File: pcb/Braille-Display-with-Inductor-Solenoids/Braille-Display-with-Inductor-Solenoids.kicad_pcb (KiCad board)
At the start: 2 copper layers, 58.2 x 57.4 mm, 56 parts, among them J1 Screw_Terminal_01x02, J2 Screw_Terminal_01x02, J3 Screw_Terminal_01x02, U1 RP2040-Zero, U2 TPIC6595, U3 TPIC6595, U4 TPIC6595

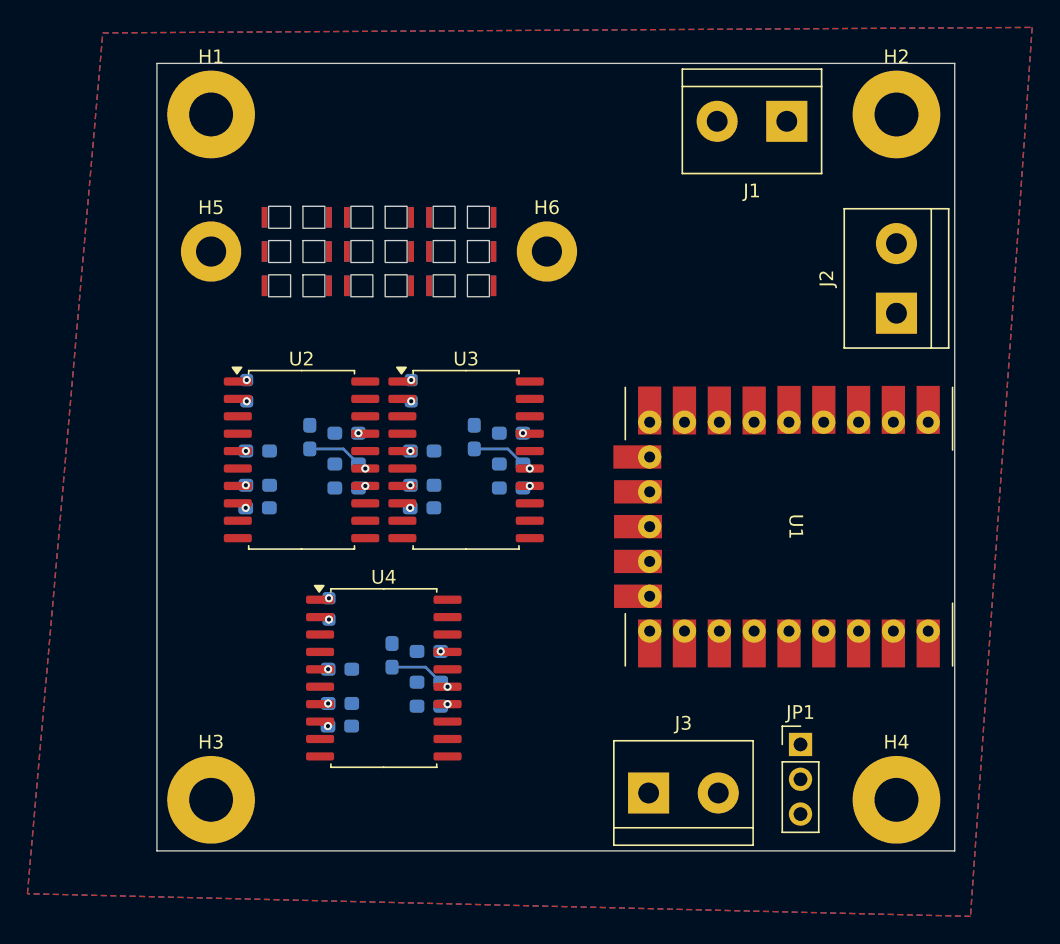
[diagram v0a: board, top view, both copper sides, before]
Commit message: Update net class rules for routing
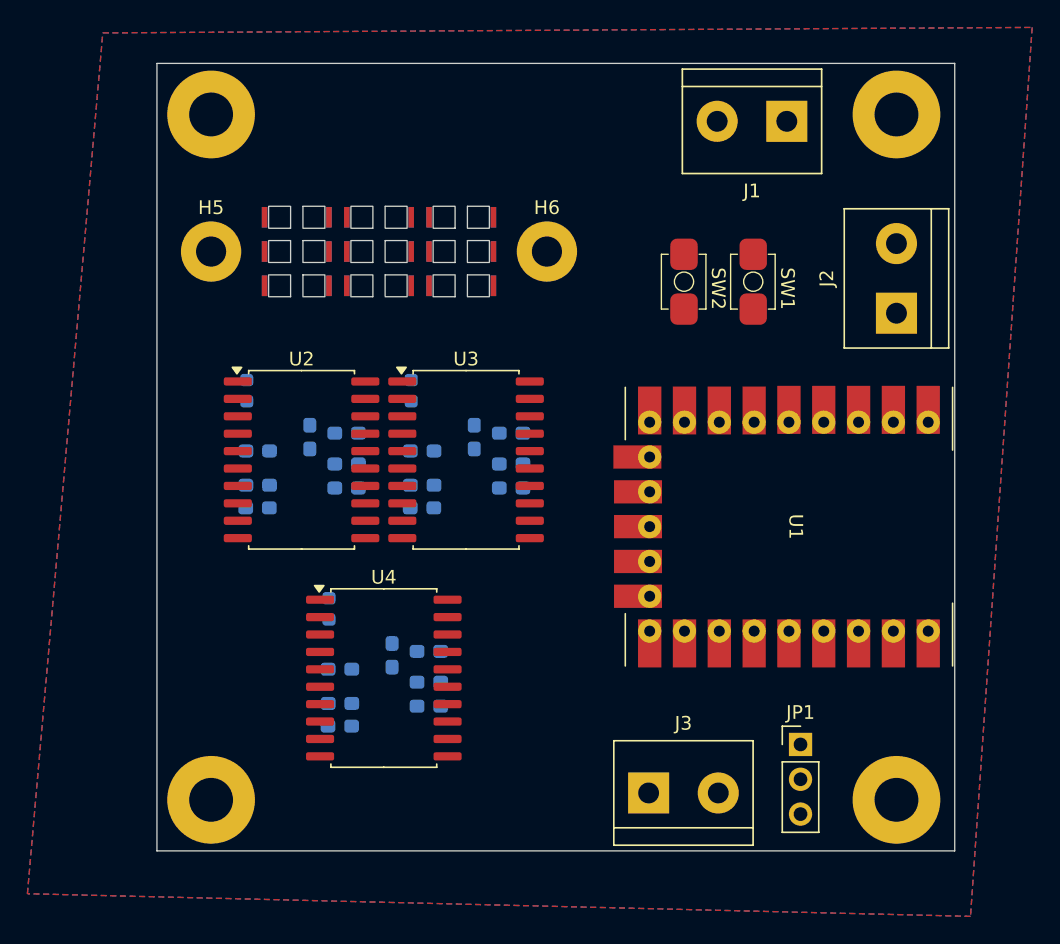
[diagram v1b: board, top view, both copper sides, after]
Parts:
- added SW1: SW_Push, 00-project-footprint-lib:PushButtonSMD_2.93x3.9, F.Cu at (134.6, 104.7)
- added SW2: SW_Push, 00-project-footprint-lib:PushButtonSMD_2.93x3.9, F.Cu at (129.5, 104.7)
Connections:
- U1 pad 5: unconnected-(U1-GP28-Pad5) -> /SW_1
- U1 pad 6: unconnected-(U1-GP27-Pad6) -> /SW_2
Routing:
- net /Braille_Cell2/DOT3_A: track 4.01 -> 0.00 mm, vias 1 -> 0
- net /Braille_Cell1/DOT3_A: track 4.01 -> 0.00 mm, vias 1 -> 0
- net /Braille_Cell/DOT3_A: track 4.01 -> 0.00 mm, vias 1 -> 0
- net VDC: vias 3 -> 0
- net Net-(U4-~{SRCLR}): vias 1 -> 0
- net Net-(U3-~{SRCLR}): vias 1 -> 0
- net Net-(U2-~{SRCLR}): vias 1 -> 0
- net GND: vias 3 -> 0
- net /Braille_Cell2/DOT6_B: vias 1 -> 0
- net /Braille_Cell2/DOT3_B: vias 1 -> 0
- net /Braille_Cell2/DOT2_B: vias 1 -> 0
- net /Braille_Cell2/DOT1_B: vias 1 -> 0
- net /Braille_Cell1/DOT6_B: vias 1 -> 0
- net /Braille_Cell1/DOT3_B: vias 1 -> 0
- net /Braille_Cell1/DOT2_B: vias 1 -> 0
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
